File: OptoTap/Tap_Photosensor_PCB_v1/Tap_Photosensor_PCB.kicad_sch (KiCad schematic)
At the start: 7 parts, among them J1 Conn_01x01_Male, J2 Conn_01x01_Male, J3 Conn_01x01_Male, U1 OPB961N51

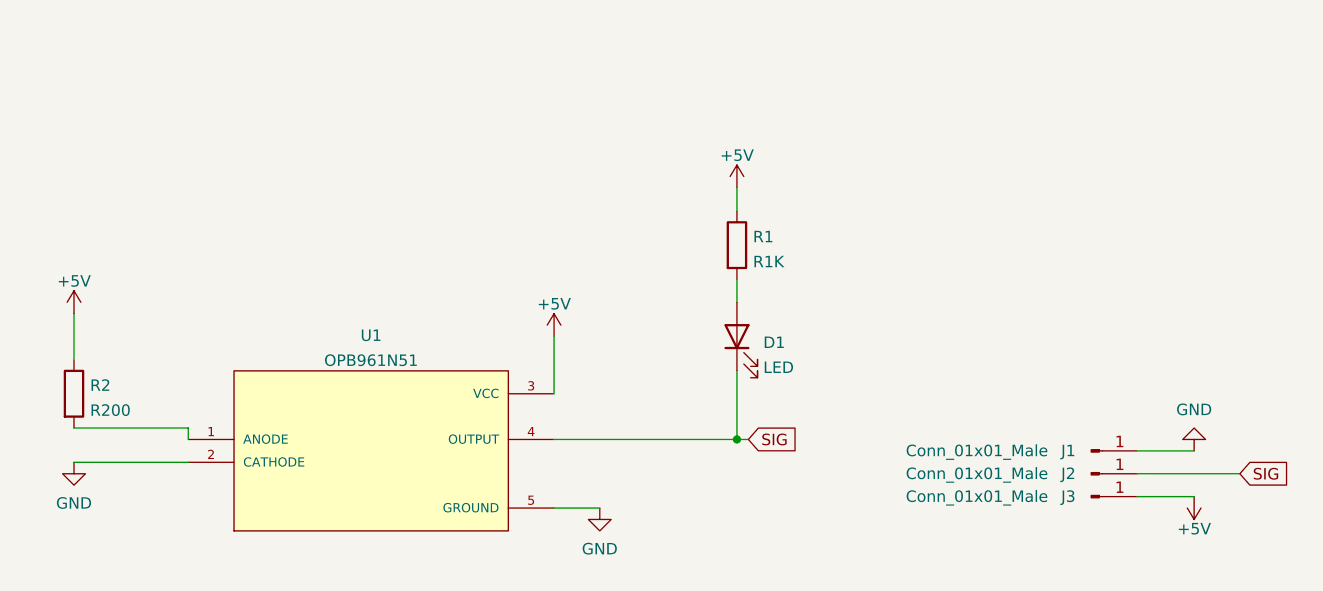
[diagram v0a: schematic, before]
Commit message: updated kicad files with proper resistor values
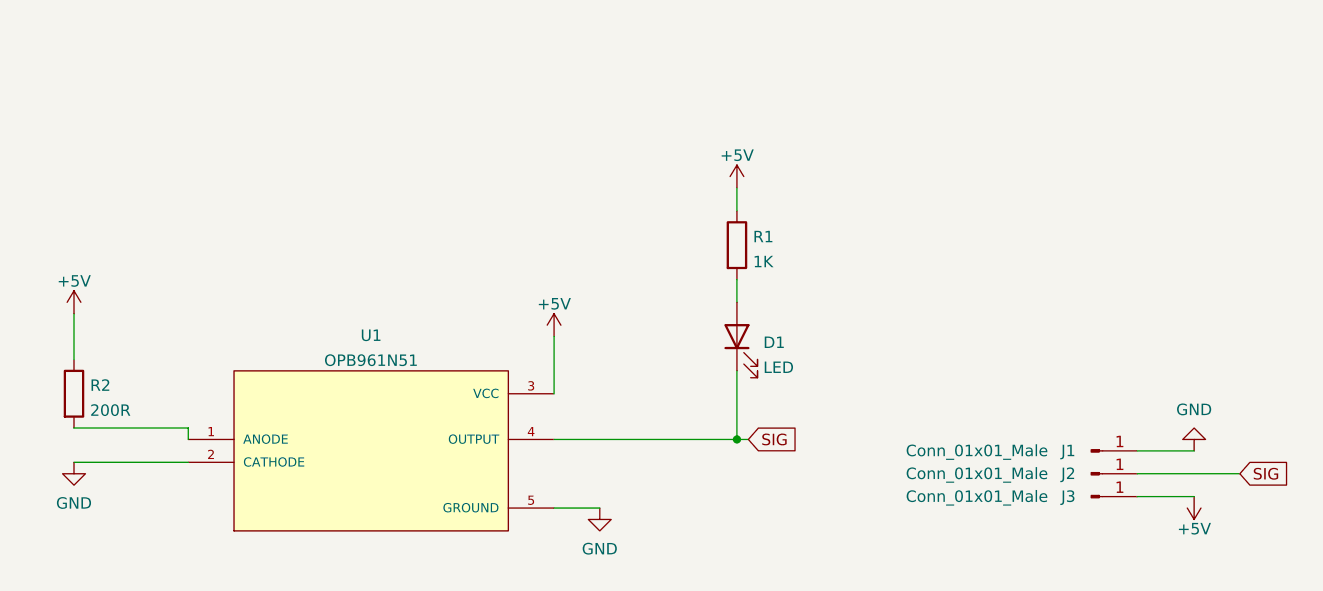
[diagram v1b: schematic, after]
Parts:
- R1: value R1K -> 1K
- R2: value R200 -> 200R
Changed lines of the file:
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@@
       (effects (font (size 1.27 1.27)) (justify left))
     )
-    (property "Value" "R200" (id 1) (at 105.918 76.7966 0)
+    (property "Value" "200R" (id 1) (at 105.918 76.7966 0)
       (effects (font (size 1.27 1.27)) (justify left))
     )
@@
       (effects (font (size 1.27 1.27)) (justify left))
     )
-    (property "Value" "R1K" (id 1) (at 179.578 60.2866 0)
+    (property "Value" "1K" (id 1) (at 179.578 60.2866 0)
       (effects (font (size 1.27 1.27)) (justify left))
     )
@@
     )
     (path "/dbb9bcbf-c2e0-477c-8d37-a9e225856a7d"
-      (reference "R1") (unit 1) (value "R1K") (footprint "Resistor_SMD:R_0805_2012Metric")
+      (reference "R1") (unit 1) (value "1K") (footprint "Resistor_SMD:R_0805_2012Metric")
     )
     (path "/42af5c76-1be1-40a2-9d2a-448b0eb158cf"
-      (reference "R2") (unit 1) (value "R200") (footprint "Resistor_SMD:R_0805_2012Metric")
+      (reference "R2") (unit 1) (value "200R") (footprint "Resistor_SMD:R_0805_2012Metric")
     )
     (path "/a3d4a3b8-80b2-4158-b88b-eda5110f79c7"

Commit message: updated OptoTap boards
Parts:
- removed D1: LED, LED_SMD:LED_0805_2012Metric, symbol Device:LED
- added D1: XL-1615RGBC, LED_SMD:LED_0606_1432, symbol LED:XL-1615RBGC
- added JP1: SolderJumper_2_Bridged, Jumper:SolderJumper-2_P1.3mm_Bridged_RoundedPad1.0x1.5mm, symbol Jumper:SolderJumper_2_Bridged
- R1: LCSC (none) -> C17513
- R2: LCSC (none) -> C17540
- U1: value OPB961N51 -> OPB961N5/EE-SX398; footprint OPTO_OPB961N51 -> footprints:OPTO_EE-SX398_OPB666N; symbol OPB961N51:OPB961N51 -> EE-SX398:EE-SX398_OPBxxx; MANUFACTURER TT Electronics -> Omron; MAXIMUM_PACKAGE_HEIGHT 10.8mm -> 10.2 mm; PARTREV D -> NA; STANDARD IPC-7351B -> Manufacturer Recommendations
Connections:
- net +5V: now also JP1.2 (B); no longer R1.1
- net GND: now also D1.3 (B)
- net SIG: now also D1.1 (R)
- net at R1.2: now also D1.2 (A)
- new net: JP1.1 (A), R1.1
- no-connect marks 0 -> 1
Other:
- moved on the sheet: R1, R2

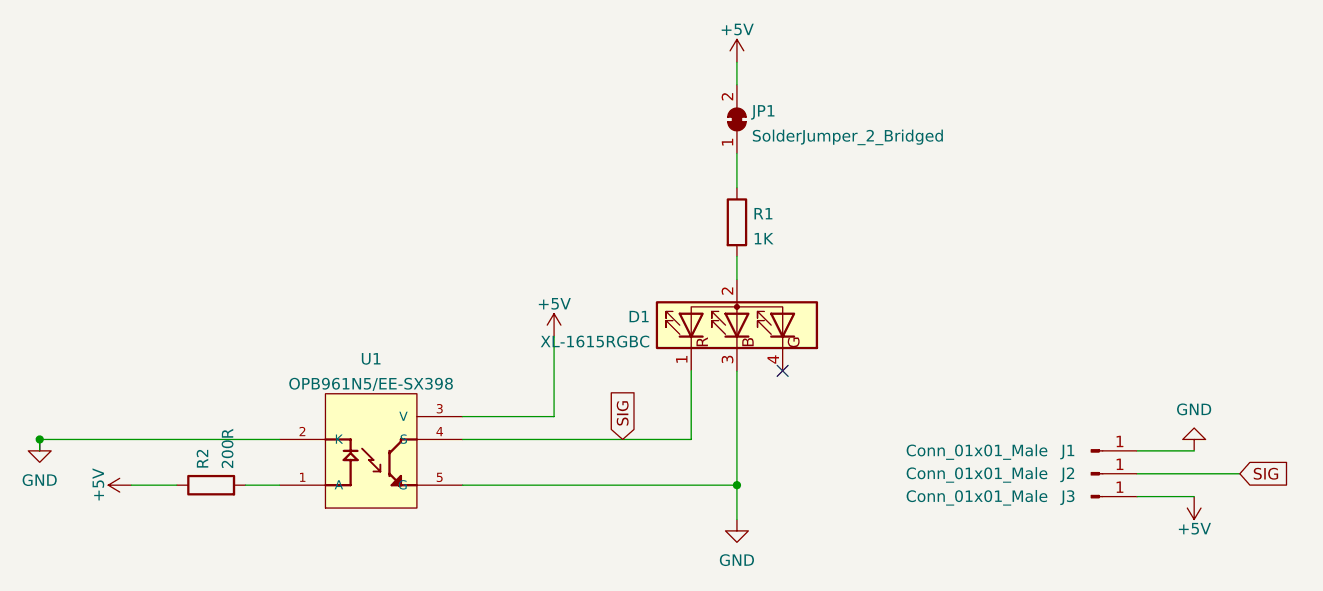
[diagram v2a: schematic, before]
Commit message: Opto24 (#68)
* updated OptoTap boards

* updated inductor info

* updated STEP and kicad

* updated README with LED ordering info

* fixed bad save
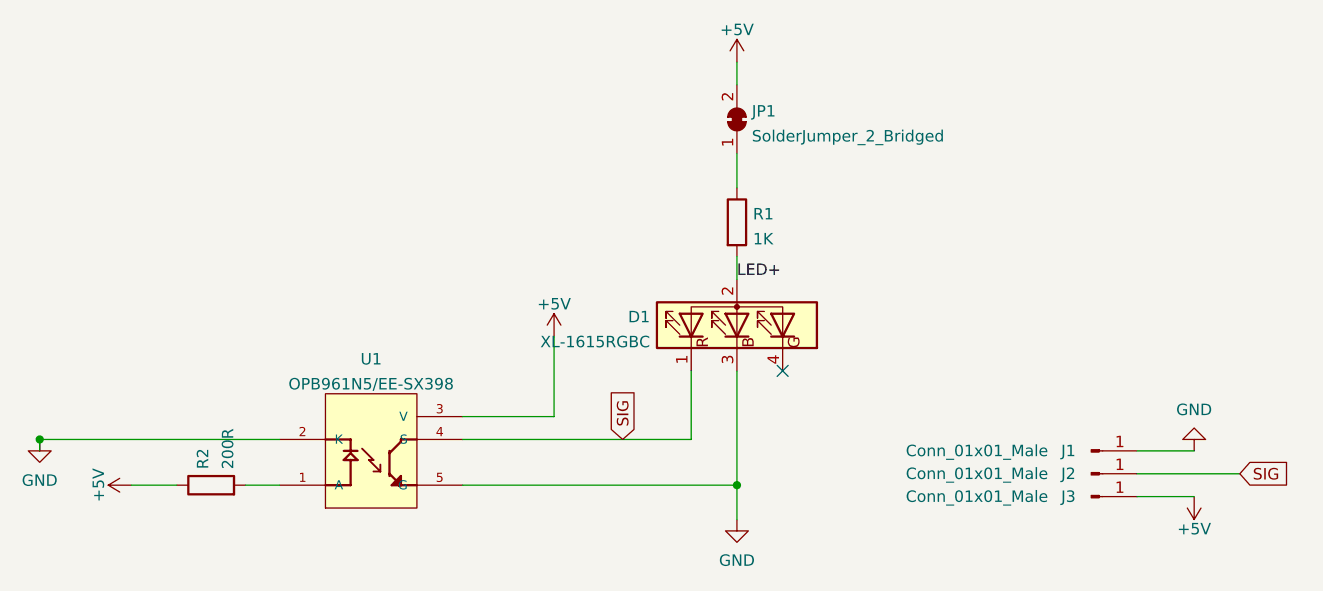
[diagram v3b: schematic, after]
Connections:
- net LED+: now reaches D1.2 (A), R1.2
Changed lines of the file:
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@@
     (stroke (width 0) (type default))
+  )
+  (label "LED+" (at 177.8 62.23 0) (fields_autoplaced)
+    (effects (font (size 1.27 1.27)) (justify left bottom))
   )
   (global_label "SIG" (shape input) (at 233.68 83.82 0) (fields_autoplaced)
